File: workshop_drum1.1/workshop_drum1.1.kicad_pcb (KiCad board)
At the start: 2 copper layers, 87.4 x 56.9 mm, 41 parts, among them J1 9v_Battery_Clip, J2 Trigger_Input, J3 Output, U1 LM358, U2 7414, U3 78L05

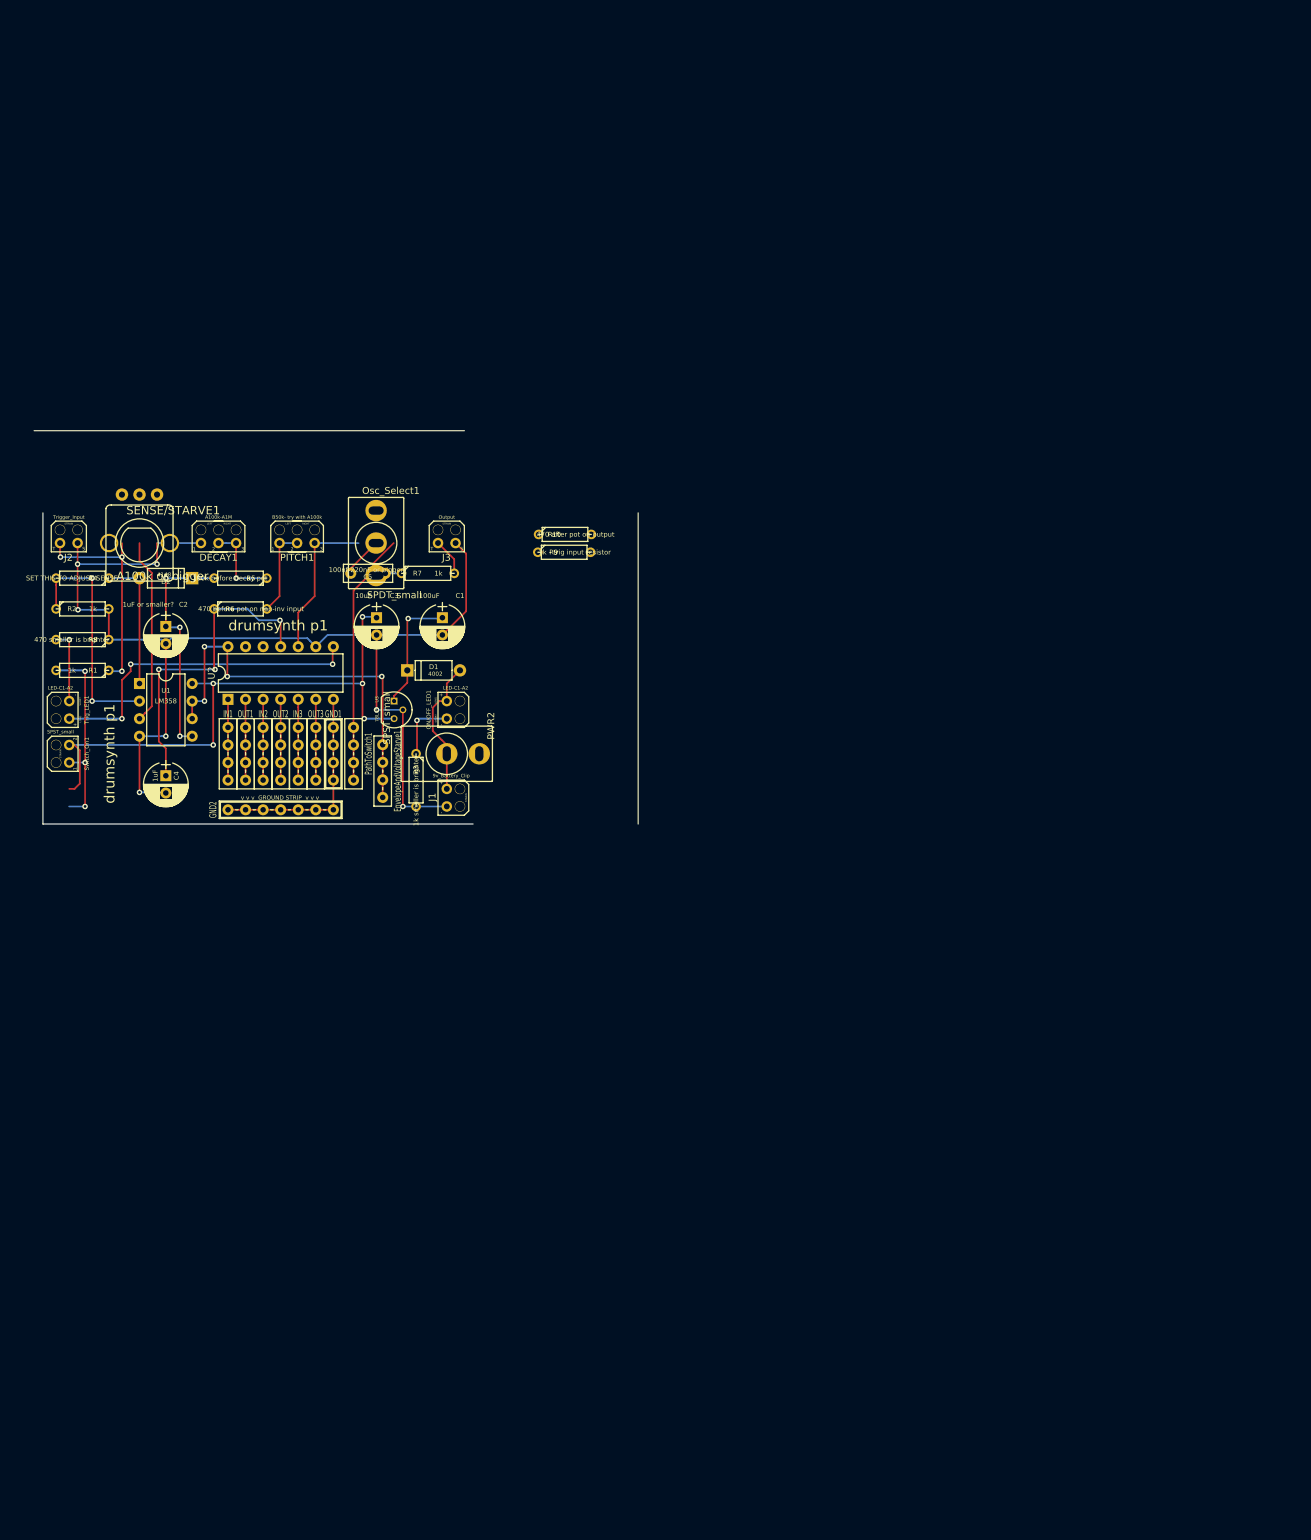
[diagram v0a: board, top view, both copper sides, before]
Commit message: P1.1 started working on breadboard strip
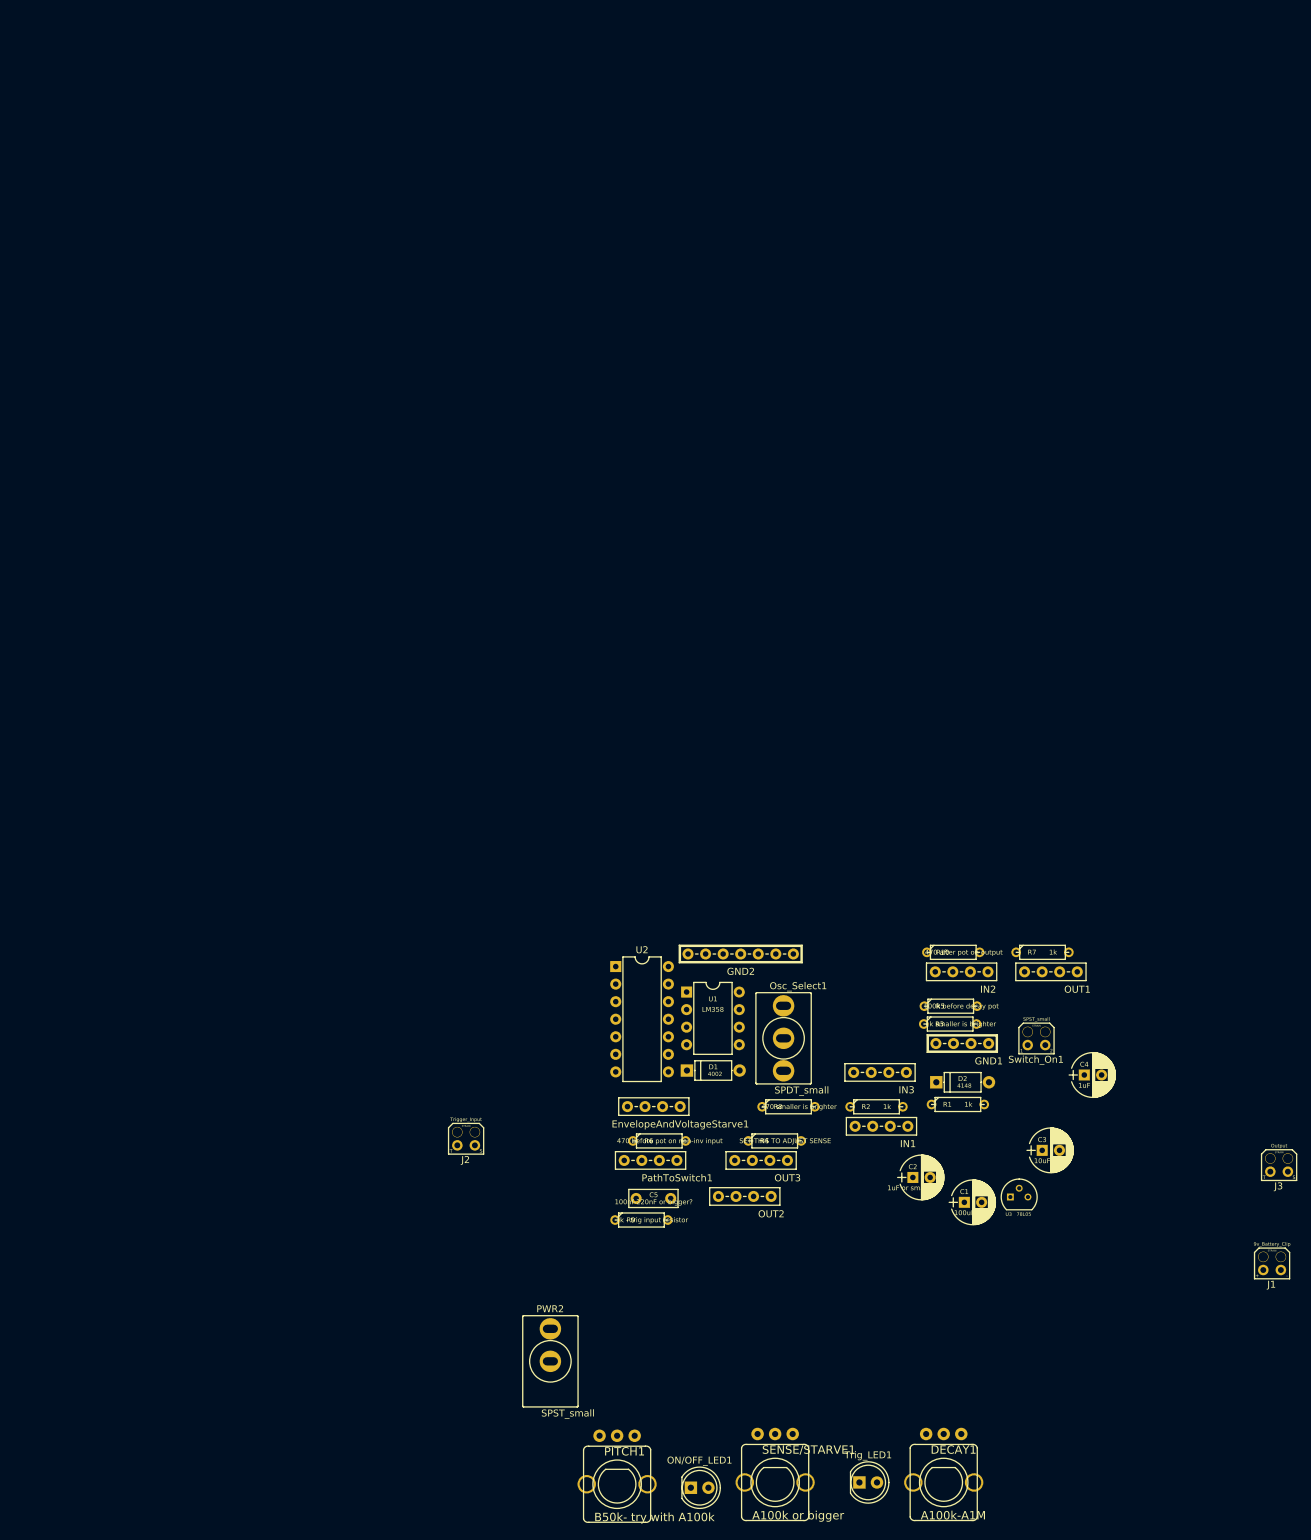
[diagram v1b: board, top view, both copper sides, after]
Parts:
- DECAY1, PITCH1: footprint zfoot:Pot_Wired -> zfoot:POT-9MM-ALPHA
- ON/OFF_LED1, Trig_LED1: footprint zfoot:LED_wired -> zfoot:LED_D5.0mm
- moved DECAY1 171.7 mm to (130.3, 95.2)
- moved SENSE/STARVE1 164.1 mm to (105.9, 95.2)
- moved Trig_LED1 159.9 mm to (118.1, 95.2), turned to 0 degrees
- moved J3 150.9 mm to (178.8, 50.3)
- moved Switch_On1 146.1 mm to (143.7, 32.0), turned to 0 degrees
- moved PITCH1 143.8 mm to (83.1, 95.5)
- moved R1 141.4 mm to (132.4, 40.6), turned to 0 degrees
- moved C4 139.7 mm to (150.6, 36.3), turned to 0 degrees
- moved J1 137.6 mm to (177.8, 64.5), turned to 0 degrees
- moved R2 135.6 mm to (120.6, 40.9)
- moved C2 134.3 mm to (125.8, 51.1), turned to 0 degrees
- moved D2 130.0 mm to (129.2, 37.4), turned to 0 degrees
- moved R4 129.1 mm to (105.9, 45.8), turned to 0 degrees
- moved C3 123.3 mm to (144.5, 47.2), turned to 0 degrees
- moved R8 122.5 mm to (107.8, 40.9), turned to 0 degrees
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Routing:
- net GND: track 200.2 -> 0.00 mm, vias 7 -> 0
- net +5V: track 84.1 -> 0.00 mm, vias 5 -> 0
- net Net-(EnvelopeAndVoltageStarve1-Pad1): track 60.0 -> 0.00 mm, vias 4 -> 0
- net Net-(Trig_LED1-Pad2): track 47.8 -> 0.00 mm, vias 3 -> 0
- net Net-(C4-Pad1): track 46.8 -> 0.00 mm, vias 3 -> 0
- net Net-(Osc_Select1-Pad3): track 36.7 -> 0.00 mm
- net Net-(R2-Pad1): track 34.3 -> 0.00 mm, vias 2 -> 0
- net Net-(C2-Pad1): track 33.6 -> 0.00 mm, vias 3 -> 0
- net Net-(J2-Pad1): track 31.4 -> 0.00 mm, vias 3 -> 0
- net Net-(R1-Pad2): track 28.4 -> 0.00 mm, vias 3 -> 0
- net Net-(SENSE/STARVE1-Pad2): track 26.9 -> 0.00 mm
- net Net-(Osc_Select1-Pad1): track 22.3 -> 0.00 mm
- net Net-(D2-Pad2): track 19.7 -> 0.00 mm
- net Net-(C1-Pad1): track 17.8 -> 0.00 mm, vias 1 -> 0
- net Net-(D1-Pad2): track 13.9 -> 0.00 mm
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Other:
- board outline removed
- rule pad_to_mask_clearance: 0.2 -> 0
- board text removed: "drumsynth p1"
- board text removed: "v v v GROUND STRIP v v v"

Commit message: re organizing boards with breakout footprints
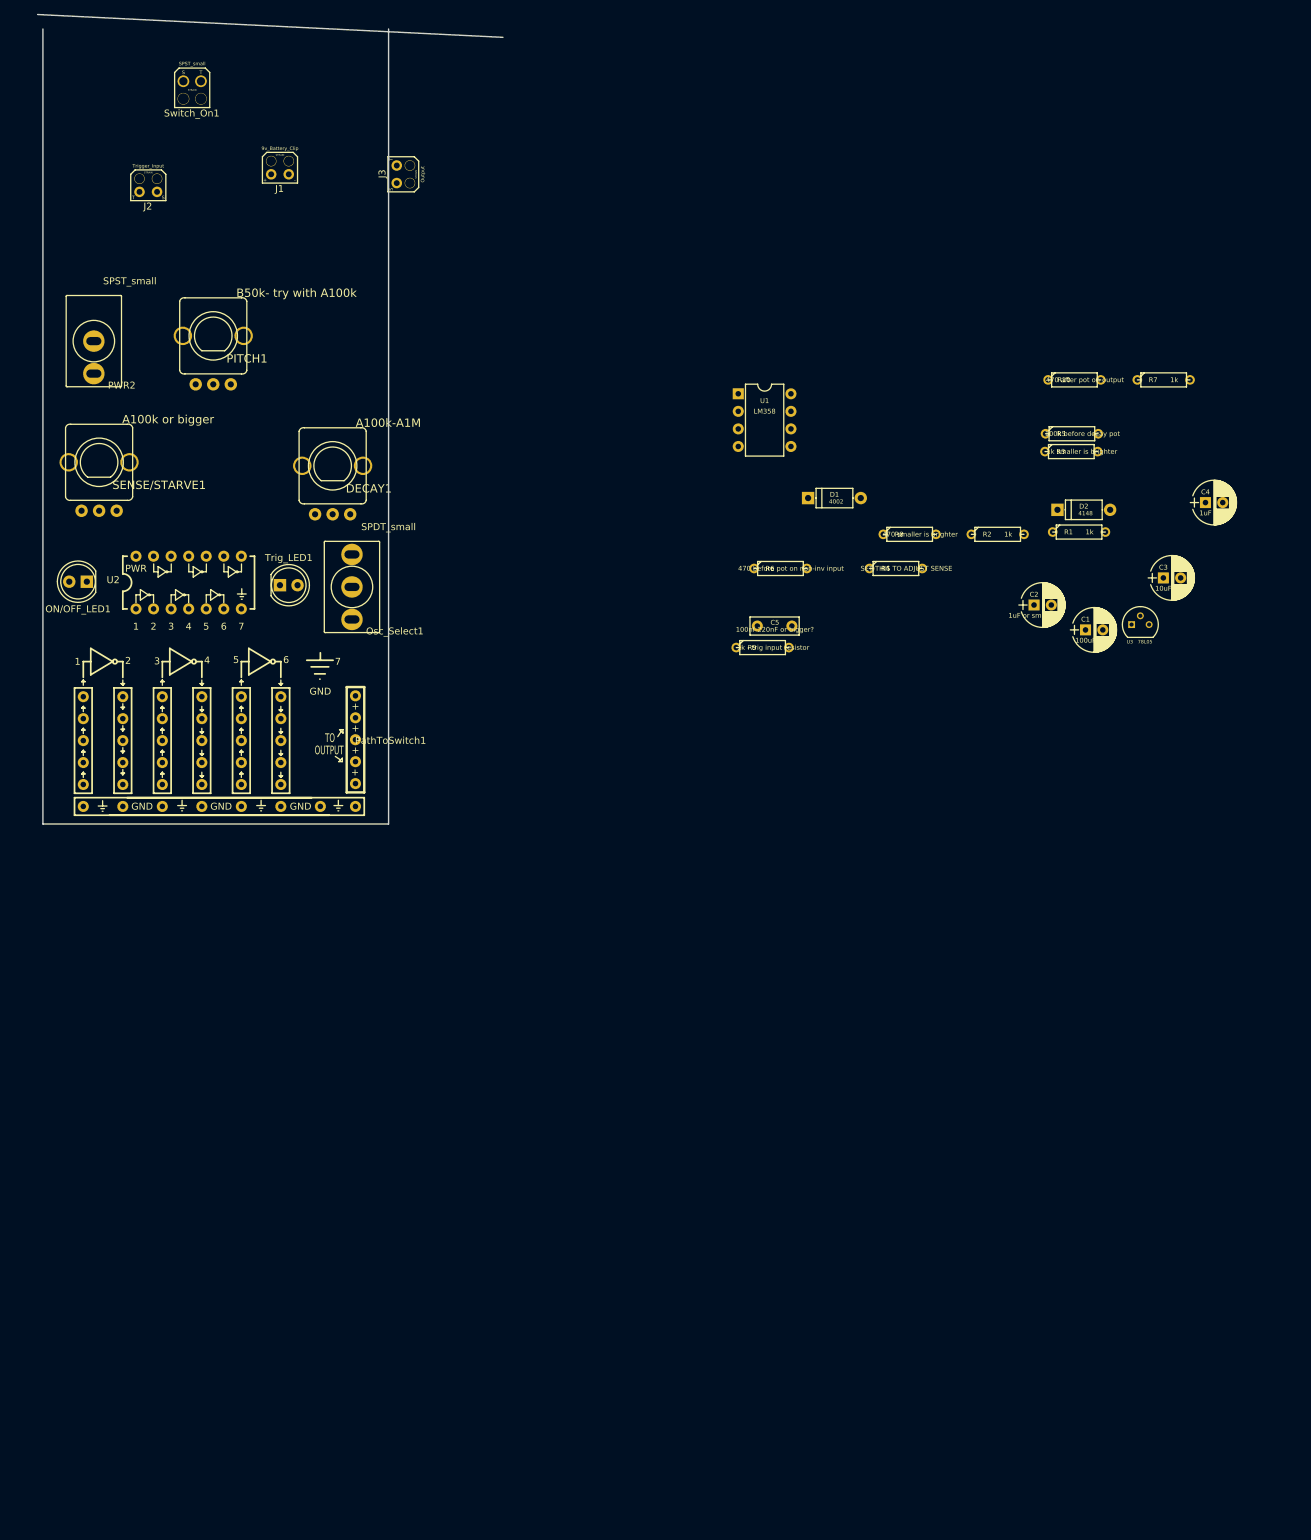
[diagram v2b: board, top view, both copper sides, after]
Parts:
- removed EnvelopeAndVoltageStarve1: PWRStrip, zfoot:BreadBoardStrip_4
- removed GND1: GNDStrip, zfoot:BreadBoardStripBold_4
- removed GND2: GNDStrip, zfoot:BreadBoardStripBold_7
- removed IN1, IN2, IN3, OUT1, OUT2, OUT3: BreadBoardStrip, zfoot:BreadBoardStrip_4
- PathToSwitch1: footprint zfoot:BreadBoardStrip_4 -> zfoot:BREAKOUTswitch
- Switch_On1: footprint zfoot:SPST_Wired -> zfoot:Jack_Instrument_Bigger
- U2: footprint 4ms-footprints:DIP-14_W7.62mm -> zfoot:BREAKOUT
- moved J1 213.8 mm to (34.3, -94.0)
- moved J3 192.6 mm to (51.2, -94.0), turned to 270 degrees
- moved Switch_On1 185.3 mm to (21.6, -107.4), turned to 180 degrees
- moved SENSE/STARVE1 177.0 mm to (8.13, -52.3), turned to 180 degrees
- moved PITCH1 176.1 mm to (24.6, -70.6), turned to 180 degrees
- moved DECAY1 171.6 mm to (41.9, -51.8), turned to 180 degrees
- moved PWR2 161.7 mm to (7.37, -69.8), turned to 180 degrees
- moved ON/OFF_LED1 157.5 mm to (6.35, -35.1), turned to 180 degrees
- moved Trig_LED1 154.5 mm to (34.3, -34.5)
- moved J2 145.4 mm to (15.2, -91.4)
- moved Osc_Select1 90.3 mm to (44.7, -34.3), turned to 180 degrees
- moved U1 86.9 mm to (100.6, -62.2)
- moved C1 84.6 mm to (150.8, -28.1)
- moved C2 84.6 mm to (143.4, -31.7)
- moved C3 84.6 mm to (162.1, -35.6)
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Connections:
- U1 pad 6: Net-(EnvelopeAndVoltageStarve1-Pad1) -> Net-(U1-Pad6)
- U1 pad 7: Net-(EnvelopeAndVoltageStarve1-Pad1) -> Net-(U1-Pad6)
- U2 pad 10: Net-(Osc_Select1-Pad1) -> (no net)
- U2 pad 11: Net-(C4-Pad1) -> (no net)
- U2 pad 12: Net-(U2-Pad12) -> (no net)
- U2 pad 13: Net-(U2-Pad13) -> (no net)
- U2 pad 14: Net-(EnvelopeAndVoltageStarve1-Pad1) -> (no net)
- U2 pad 7: GND -> (no net)
- U2 pad 8: Net-(Trig_LED1-Pad2) -> (no net)
- U2 pad 9: GND -> (no net)
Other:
- board outline added: 67.3 x 117.1 mm
